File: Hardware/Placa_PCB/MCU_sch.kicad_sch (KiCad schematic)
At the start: 0 parts

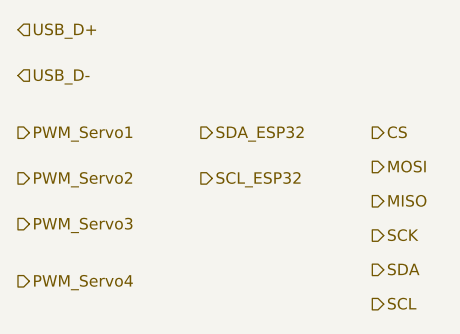
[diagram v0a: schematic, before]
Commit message: Agregando Level Shifter al PWM del Servo
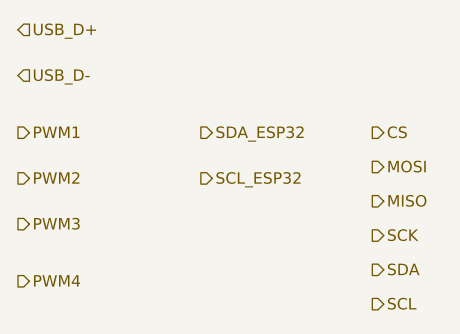
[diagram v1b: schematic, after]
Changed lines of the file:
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@@
 		)
 	)
-	(hierarchical_label "PWM_Servo4"
+	(hierarchical_label "PWM4"
 		(shape output)
 		(at 62.23 88.9 0)
@@
 		)
 	)
-	(hierarchical_label "PWM_Servo1"
+	(hierarchical_label "PWM1"
 		(shape output)
 		(at 62.23 72.39 0)
@@
 		)
 	)
-	(hierarchical_label "PWM_Servo3"
+	(hierarchical_label "PWM3"
 		(shape output)
 		(at 62.23 82.55 0)
@@
 		)
 	)
-	(hierarchical_label "PWM_Servo2"
+	(hierarchical_label "PWM2"
 		(shape output)
 		(at 62.23 77.47 0)

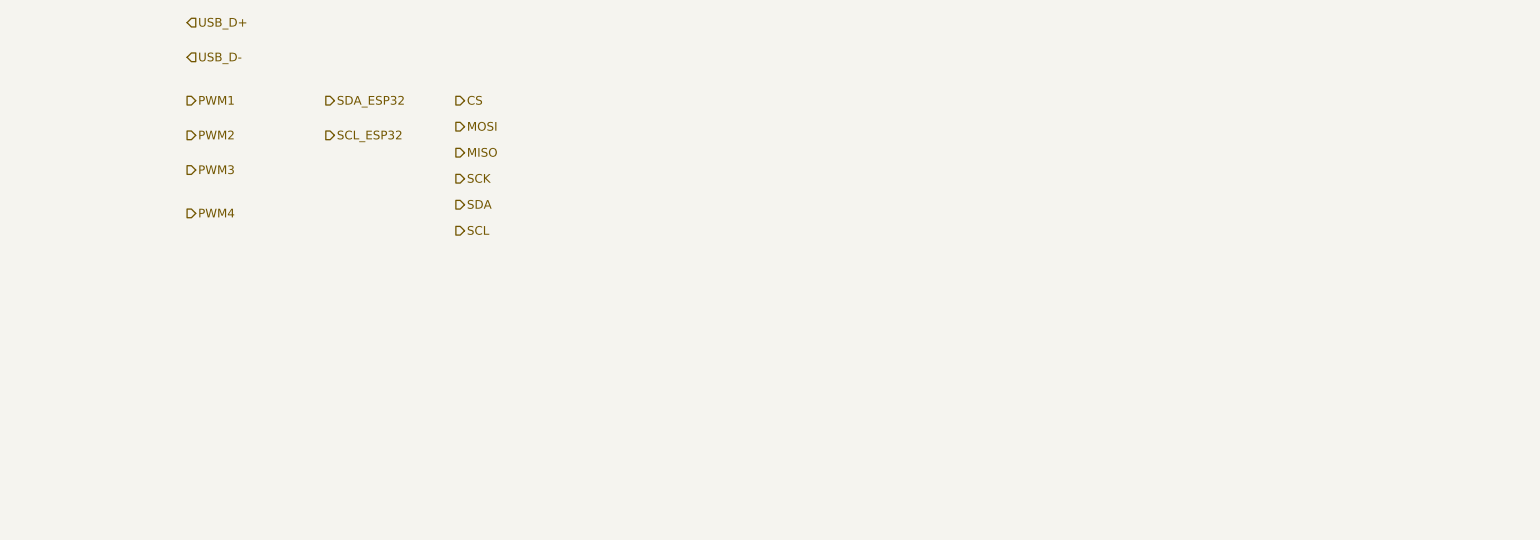
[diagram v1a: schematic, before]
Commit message: Agregando MCU al esquematico
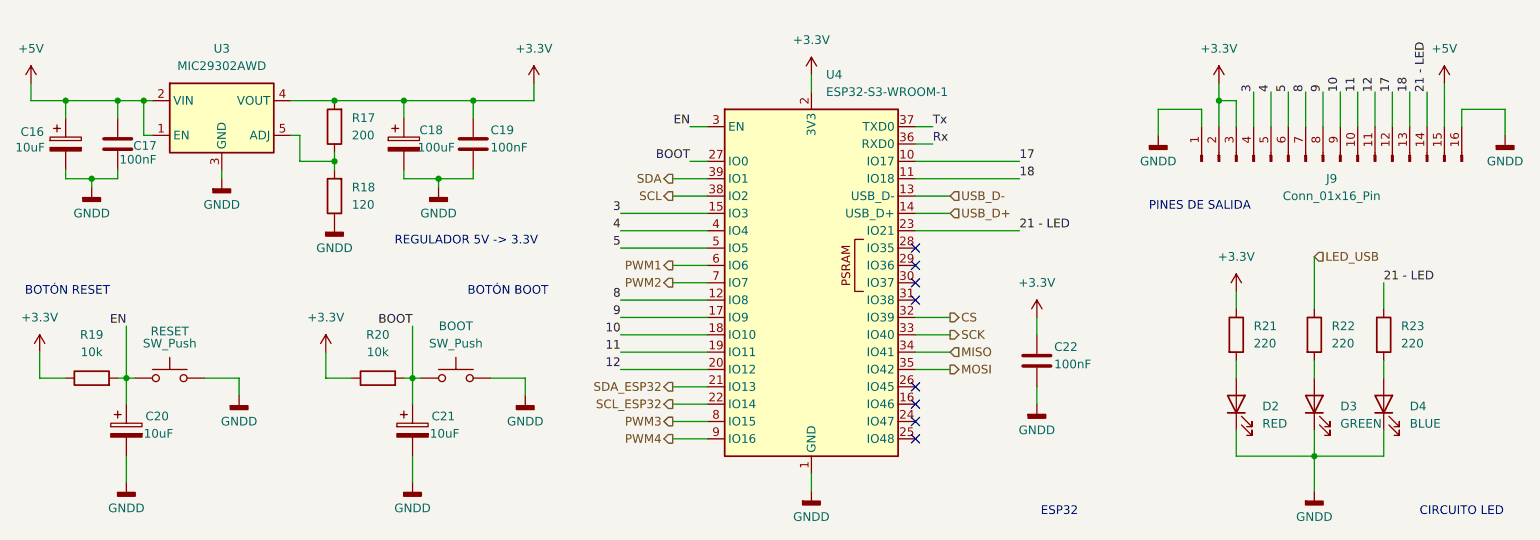
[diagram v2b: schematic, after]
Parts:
- added BOOT, RESET: SW_Push, Button_Switch_SMD:SW_SPST_TL3342, symbol Switch:SW_Push
- added C16, C20, C21: 10uF, symbol Device:C_Polarized
- added C17, C19, C22: 100nF, symbol Device:C
- added C18: 100uF, symbol Device:C_Polarized
- added D2: RED, symbol Device:LED
- added D3: GREEN, symbol Device:LED
- added D4: BLUE, symbol Device:LED
- added J9: Conn_01x16_Pin, symbol Connector:Conn_01x16_Pin
- added R17: 200, symbol Device:R
- added R18: 120, symbol Device:R
- added R19, R20: 10k, symbol Device:R
- added R21, R22, R23: 220, symbol Device:R
- added U3: MIC29302AWD, Package_TO_SOT_SMD:TO-252-5_TabPin3, symbol Regulator_Linear:MIC29302AWD
- added U4: ESP32-S3-WROOM-1, RF_Module:ESP32-S3-WROOM-1, symbol RF_Module:ESP32-S3-WROOM-1
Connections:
- net CS: now also U4.32 (IO39)
- net MISO: now also U4.34 (IO41)
- net MOSI: now also U4.35 (IO42)
- net PWM1: now also U4.6 (IO6)
- net PWM2: now also U4.7 (IO7)
- net PWM3: now also U4.8 (IO15)
- net PWM4: now also U4.9 (IO16)
- net SCK: now also U4.33 (IO40)
- net SCL: now also U4.38 (IO2)
- net SCL_ESP32: now also U4.22 (IO14)
- net SDA: now also U4.39 (IO1)
- net SDA_ESP32: now also U4.21 (IO13)
- net USB_D+: now also U4.14 (USB_D+)
- net USB_D-: now also U4.13 (USB_D-)
- new net: R17.1, R18.2, U3.5 (ADJ)
- new net: D2.2 (A), R21.2
- new net: D4.2 (A), R23.2
- new net: D3.2 (A), R22.2
- new net +3.3V: C18.1, C19.1, C22.1, J9.2 (Pin_2), J9.3 (Pin_3), R17.2, R19.1, R20.1, R21.1, U3.4 (VOUT), U4.2 (3V3)
- new net +5V: C16.1, C17.1, J9.15 (Pin_15), U3.1 (EN), U3.2 (VIN)
- new net 10: J9.9 (Pin_9), U4.18 (IO10)
- new net 11: J9.10 (Pin_10), U4.19 (IO11)
- new net 12: J9.11 (Pin_11), U4.20 (IO12)
- new net 17: J9.12 (Pin_12), U4.10 (IO17)
- new net 18: J9.13 (Pin_13), U4.11 (IO18)
- new net 21 - LED: J9.14 (Pin_14), R23.1, U4.23 (IO21)
- new net 3: J9.4 (Pin_4), U4.15 (IO3)
- new net 4: J9.5 (Pin_5), U4.4 (IO4)
- new net 5: J9.6 (Pin_6), U4.5 (IO5)
- new net 8: J9.7 (Pin_7), U4.12 (IO8)
- new net 9: J9.8 (Pin_8), U4.17 (IO9)
- new net BOOT: BOOT.1, C21.1, R20.2, U4.27 (IO0)
- new net EN: C20.1, R19.2, RESET.1, U4.3 (EN)
- new net GNDD: BOOT.2, C16.2, C17.2, C18.2, C19.2, C20.2, C21.2, C22.2, D2.1 (K), D3.1 (K), D4.1 (K), J9.1 (Pin_1), J9.16 (Pin_16), R18.1, RESET.2, U3.3 (GND), U4.1 (GND), U4.40 (GND), U4.41 (GND)
- new net LED_USB: R22.1
- new net Rx: U4.36 (RXD0)
- new net Tx: U4.37 (TXD0)
- no-connect marks 0 -> 8
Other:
- note added: "BOTÓN BOOT"
- note added: "BOTÓN RESET"
- note added: "CIRCUITO LED"
- note added: "ESP32"
- note added: "PINES DE SALIDA"
- note added: "REGULADOR 5V -> 3.3V"

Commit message: Esquematico Final
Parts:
- removed C18: 100uF, symbol Device:C_Polarized
- removed C20, C21: 10uF, symbol Device:C_Polarized
- removed J9: Conn_01x16_Pin, symbol Connector:Conn_01x16_Pin
- added C19, C20: 10uF, Capacitor_SMD:C_0805_2012Metric_Pad1.18x1.45mm_HandSolder, symbol Device:C
- added J9: Conn_01x18_Pin, Connector_PinSocket_2.54mm:PinSocket_1x18_P2.54mm_Vertical, symbol Connector:Conn_01x18_Pin
- 3V3_POW1: renamed from D2; value RED -> GREEN; footprint (none) -> LED_SMD:LED_0805_2012Metric_Pad1.15x1.40mm_HandSolder
- 5V_POW1: renamed from D3; value GREEN -> ORANGE; footprint (none) -> LED_SMD:LED_0805_2012Metric_Pad1.15x1.40mm_HandSolder
- BOOT1: renamed from BOOT; footprint Button_Switch_SMD:SW_SPST_TL3342 -> Button_Switch_SMD:SW_Push_1P1T_NO_E-Switch_TL3301NxxxxxG
- C16, C17: footprint (none) -> Capacitor_SMD:C_0805_2012Metric_Pad1.18x1.45mm_HandSolder
- C18: renamed from C19; footprint (none) -> Capacitor_SMD:CP_Elec_6.3x5.8
- C21: renamed from C22; footprint (none) -> Capacitor_SMD:C_0805_2012Metric_Pad1.18x1.45mm_HandSolder
- PIN21: renamed from D4; value BLUE -> YELLOW; footprint (none) -> LED_SMD:LED_0805_2012Metric_Pad1.15x1.40mm_HandSolder
- R17, R18, R19, R20: footprint (none) -> Resistor_SMD:R_0805_2012Metric_Pad1.20x1.40mm_HandSolder
- R21: value 220 -> 100; footprint (none) -> Resistor_SMD:R_0805_2012Metric_Pad1.20x1.40mm_HandSolder
- R22: value 220 -> 330; footprint (none) -> Resistor_SMD:R_0805_2012Metric_Pad1.20x1.40mm_HandSolder
- R23: value 220 -> 120; footprint (none) -> Resistor_SMD:R_0805_2012Metric_Pad1.20x1.40mm_HandSolder
- RESET1: renamed from RESET; footprint Button_Switch_SMD:SW_SPST_TL3342 -> Button_Switch_SMD:SW_Push_1P1T_NO_E-Switch_TL3301NxxxxxG
- renumbered U3 to U4, U4 to U5
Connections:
- net 12 is gone; now on net SDA: U5.20 (IO12)
- net 4 is gone; now on net PWM1: U5.4 (IO4)
- net 5 is gone; now on net PWM2: U5.5 (IO5)
- net +3.3V: now also J9.2 (Pin_2), J9.3 (Pin_3)
- net +5V: now also J9.16 (Pin_16), J9.17 (Pin_17)
- net 10: now also J9.7 (Pin_7)
- net 11: now also J9.8 (Pin_8)
- net 17: now also J9.11 (Pin_11)
- net 18: now also J9.12 (Pin_12)
- net 3: now also J9.4 (Pin_4)
- net 8: now also J9.5 (Pin_5)
- net 9: now also J9.6 (Pin_6)
- net BOOT: now also C20.1
- net CS: now also U5.24 (IO47); no longer U5.32 (IO39)
- net EN: now also C19.1
- net GNDD: now also C19.2, C20.2, J9.1 (Pin_1), J9.18 (Pin_18)
- net MISO: now also U5.23 (IO21); no longer U5.34 (IO41)
- net MOSI: now also U5.22 (IO14); no longer U5.35 (IO42)
- net PWM1: no longer U5.6 (IO6)
- net PWM2: no longer U5.7 (IO7)
- net PWM3: now also U5.6 (IO6); no longer U5.8 (IO15)
- net PWM4: now also U5.7 (IO7); no longer U5.9 (IO16)
- net SCK: now also U5.25 (IO48); no longer U5.33 (IO40)
- net SCL: now also U5.21 (IO13); no longer U5.38 (IO2)
- net SCL_ESP32: now also U5.38 (IO2); no longer U5.22 (IO14)
- net SDA: no longer U5.39 (IO1)
- net SDA_ESP32: now also U5.39 (IO1); no longer U5.21 (IO13)
- net 38 - LED: now reaches U5.31 (IO38)
- net 38 - LED: now also R23.1, J9.13 (Pin_13)
- removed net 21 - LED: R23.1, U5.23 (IO21)
- net Rx renamed RX
- net RX: now also J9.15 (Pin_15)
- net Tx renamed TX
- net TX: now also J9.14 (Pin_14)
- new net 15: J9.9 (Pin_9), U5.8 (IO15)
- new net 16: J9.10 (Pin_10), U5.9 (IO16)
- no-connect marks 8 -> 9
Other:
- moved on the sheet: C18

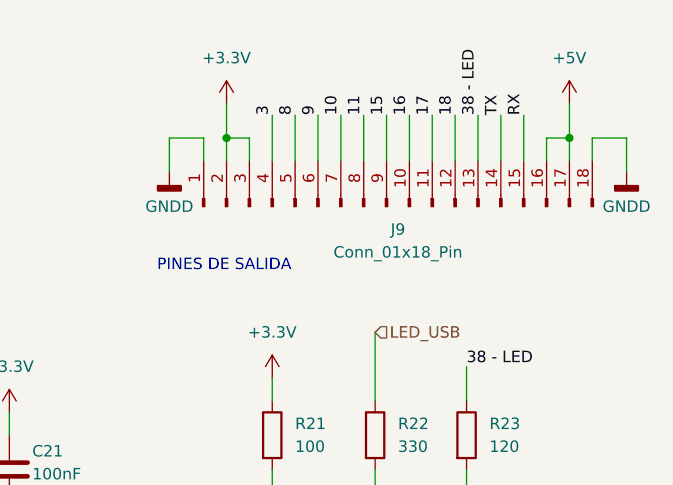
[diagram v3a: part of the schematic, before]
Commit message: Agregando huella del capacitor de 10uF y comenzando con el PCB (USB + Alimentacion)
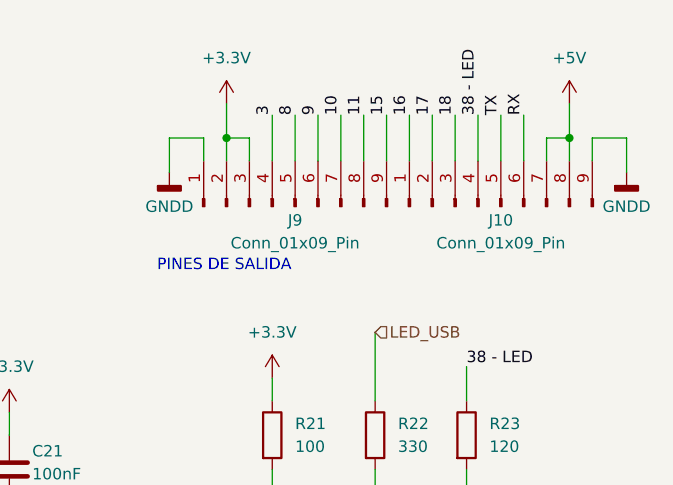
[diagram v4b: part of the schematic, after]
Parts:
- removed J9: Conn_01x18_Pin, Connector_PinSocket_2.54mm:PinSocket_1x18_P2.54mm_Vertical, symbol Connector:Conn_01x18_Pin
- added J10, J9: Conn_01x09_Pin, Connector_PinSocket_2.54mm:PinSocket_1x09_P2.54mm_Vertical, symbol Connector:Conn_01x09_Pin
- C16: footprint Capacitor_SMD:C_0805_2012Metric_Pad1.18x1.45mm_HandSolder -> Capacitor_SMD:CP_Elec_4x5.4
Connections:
- net +3.3V: now also J9.2 (Pin_2), J9.3 (Pin_3)
- net +5V: now also J10.7 (Pin_7), J10.8 (Pin_8)
- net 10: now also J9.7 (Pin_7)
- net 11: now also J9.8 (Pin_8)
- net 15: now also J9.9 (Pin_9)
- net 16: now also J10.1 (Pin_1)
- net 17: now also J10.2 (Pin_2)
- net 18: now also J10.3 (Pin_3)
- net 3: now also J9.4 (Pin_4)
- net 38 - LED: now also J10.4 (Pin_4)
- net 8: now also J9.5 (Pin_5)
- net 9: now also J9.6 (Pin_6)
- net GNDD: now also J10.9 (Pin_9), J9.1 (Pin_1)
- net RX: now also J10.6 (Pin_6)
- net TX: now also J10.5 (Pin_5)

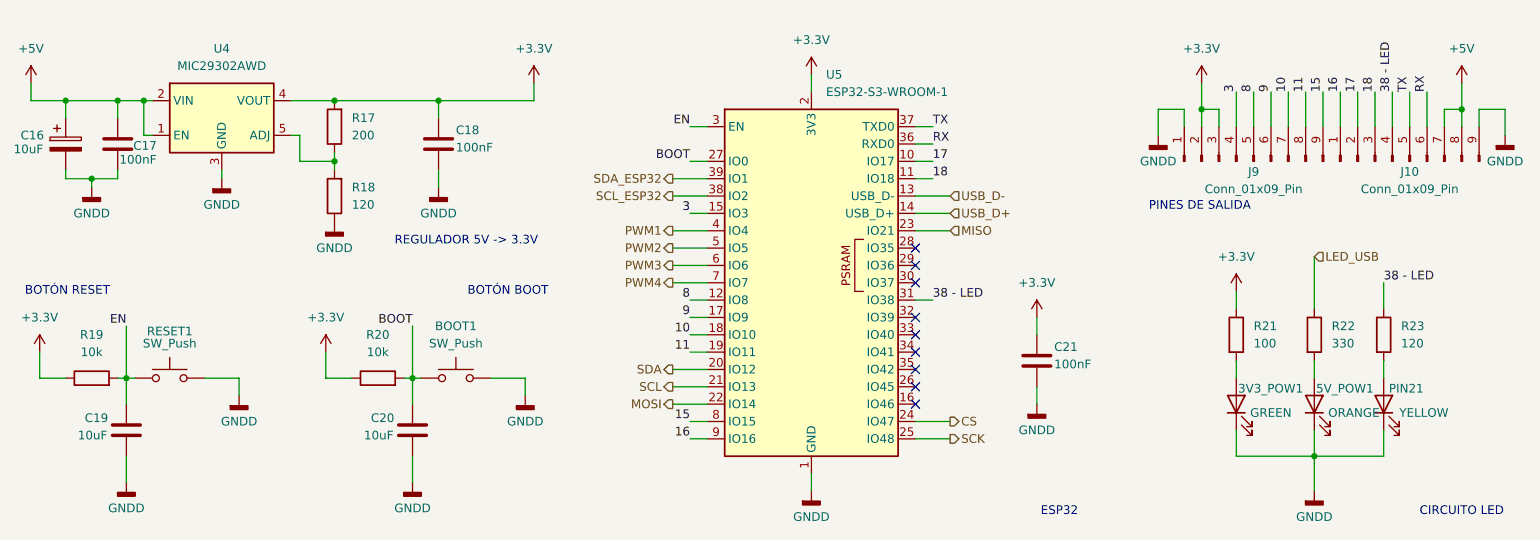
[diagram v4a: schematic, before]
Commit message: Acomodando los componentes en el PCB y cambiendo las conexiones con el ESP32
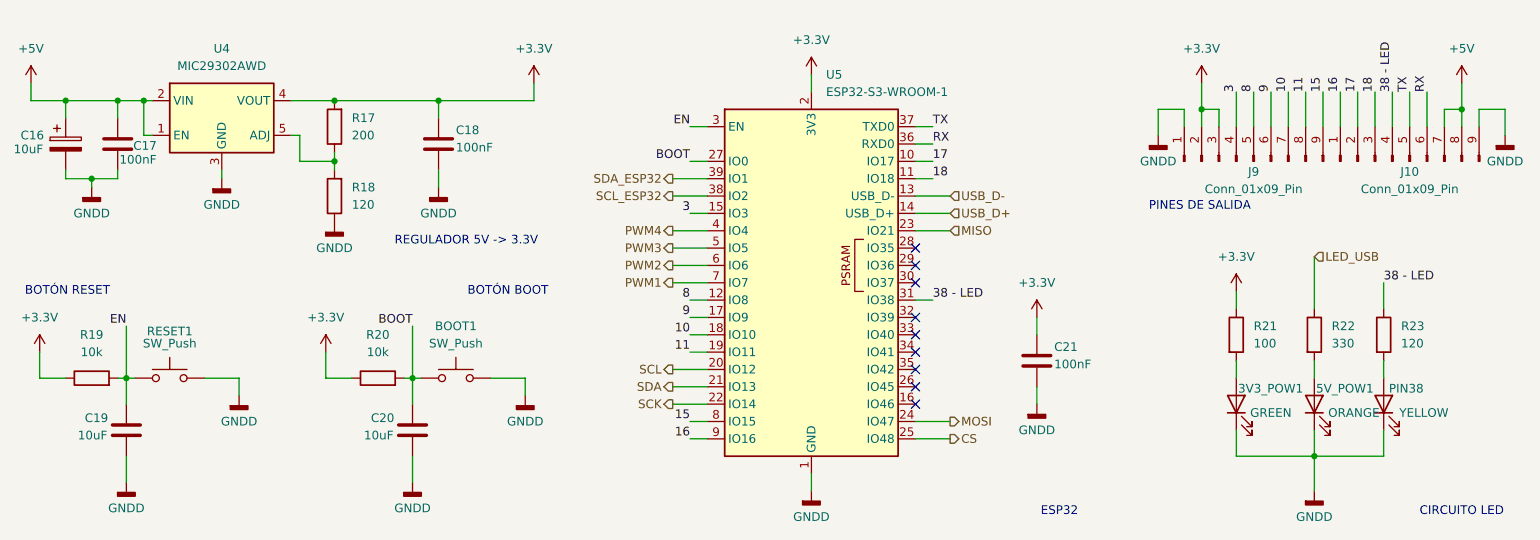
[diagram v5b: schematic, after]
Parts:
- C18: footprint Capacitor_SMD:CP_Elec_6.3x5.8 -> Capacitor_SMD:C_0805_2012Metric_Pad1.18x1.45mm_HandSolder
- renumbered PIN21 to PIN38
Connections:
- net CS: now also U5.25 (IO48); no longer U5.24 (IO47)
- net MOSI: now also U5.24 (IO47); no longer U5.22 (IO14)
- net PWM1: now also U5.7 (IO7); no longer U5.4 (IO4)
- net PWM2: now also U5.6 (IO6); no longer U5.5 (IO5)
- net PWM3: now also U5.5 (IO5); no longer U5.6 (IO6)
- net PWM4: now also U5.4 (IO4); no longer U5.7 (IO7)
- net SCK: now also U5.22 (IO14); no longer U5.25 (IO48)
- net SCL: now also U5.20 (IO12); no longer U5.21 (IO13)
- net SDA: now also U5.21 (IO13); no longer U5.20 (IO12)
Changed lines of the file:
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@@
 	(wire
 		(pts
-			(xy 255.27 73.66) (xy 251.46 73.66)
+			(xy 133.35 99.06) (xy 138.43 99.06)
 		)
 		(stroke
@@
 	(wire
 		(pts
-			(xy 135.89 106.68) (xy 138.43 106.68)
+			(xy 255.27 73.66) (xy 251.46 73.66)
 		)
 		(stroke
@@
 	(wire
 		(pts
-			(xy 248.92 69.85) (xy 248.92 73.66)
+			(xy 135.89 106.68) (xy 138.43 106.68)
 		)
 		(stroke
@@
 	(wire
 		(pts
-			(xy 227.33 124.46) (xy 227.33 129.54)
+			(xy 248.92 69.85) (xy 248.92 73.66)
 		)
 		(stroke
@@
 	(wire
 		(pts
-			(xy 135.89 81.28) (xy 138.43 81.28)
+			(xy 227.33 124.46) (xy 227.33 129.54)
 		)
 		(stroke
@@
 	(wire
 		(pts
-			(xy 133.35 116.84) (xy 138.43 116.84)
+			(xy 135.89 81.28) (xy 138.43 81.28)
 		)
 		(stroke
@@
 	(wire
 		(pts
-			(xy 237.49 110.49) (xy 237.49 113.03)
+			(xy 133.35 116.84) (xy 138.43 116.84)
 		)
 		(stroke
@@
 	(wire
 		(pts
-			(xy 133.35 93.98) (xy 138.43 93.98)
+			(xy 237.49 110.49) (xy 237.49 113.03)
 		)
 		(stroke
@@
 	(wire
 		(pts
-			(xy 133.35 91.44) (xy 138.43 91.44)
-		)
-		(stroke
-			(width 0)
-			(type default)
-		)
-	)
-	(wire
-		(pts
 			(xy 83.82 72.39) (xy 99.06 72.39)
 		)
@@
 	(wire
 		(pts
+			(xy 133.35 93.98) (xy 138.43 93.98)
+		)
+		(stroke
+			(width 0)
+			(type default)
+		)
+	)
+	(wire
+		(pts
 			(xy 106.68 113.03) (xy 111.76 113.03)
 		)
@@
 	(wire
 		(pts
-			(xy 133.35 99.06) (xy 138.43 99.06)
-		)
-		(stroke
-			(width 0)
-			(type default)
-		)
-	)
-	(wire
-		(pts
 			(xy 78.74 77.47) (xy 78.74 81.28)
 		)
@@
 	(wire
 		(pts
-			(xy 133.35 96.52) (xy 138.43 96.52)
-		)
-		(stroke
-			(width 0)
-			(type default)
-		)
-	)
-	(wire
-		(pts
 			(xy 44.45 83.82) (xy 48.26 83.82)
 		)
@@
 	(wire
 		(pts
+			(xy 133.35 96.52) (xy 138.43 96.52)
+		)
+		(stroke
+			(width 0)
+			(type default)
+		)
+	)
+	(wire
+		(pts
 			(xy 231.14 71.12) (xy 231.14 76.2)
 		)
@@
 	(wire
 		(pts
+			(xy 133.35 91.44) (xy 138.43 91.44)
+		)
+		(stroke
+			(width 0)
+			(type default)
+		)
+	)
+	(wire
+		(pts
 			(xy 48.26 83.82) (xy 48.26 85.09)
 		)
@@
 	(hierarchical_label "PWM4"
 		(shape output)
-		(at 133.35 99.06 180)
+		(at 133.35 91.44 180)
 		(effects
 			(font
@@
 	(hierarchical_label "SDA"
 		(shape output)
-		(at 133.35 111.76 180)
+		(at 133.35 114.3 180)
 		(effects
 			(font
@@
 	(hierarchical_label "CS"
 		(shape output)
-		(at 173.99 119.38 0)
+		(at 173.99 121.92 0)
 		(effects
 			(font
@@
 	(hierarchical_label "MOSI"
 		(shape output)
-		(at 133.35 116.84 180)
+		(at 173.99 119.38 0)
 		(effects
 			(font
 				(size 1.27 1.27)
 			)
-			(justify right)
+			(justify left)
 		)
 	)
@@
 	(hierarchical_label "PWM1"
 		(shape output)
-		(at 133.35 91.44 180)
+		(at 133.35 99.06 180)
 		(effects
 			(font
@@
 	(hierarchical_label "SCL"
 		(shape output)
-		(at 133.35 114.3 180)
+		(at 133.35 111.76 180)
 		(effects
 			(font
@@
 	(hierarchical_label "PWM2"
 		(shape output)
-		(at 133.35 93.98 180)
+		(at 133.35 96.52 180)
 		(effects
 			(font
@@
 	(hierarchical_label "SCK"
 		(shape output)
-		(at 173.99 121.92 0)
+		(at 133.35 116.84 180)
 		(effects
 			(font
 				(size 1.27 1.27)
 			)
-			(justify left)
+			(justify right)
 		)
 	)
 	(hierarchical_label "PWM3"
 		(shape output)
-		(at 133.35 96.52 180)
+		(at 133.35 93.98 180)
 		(effects
 			(font
@@
 		(on_board yes)
 		(dnp no)
-		(property "Reference" "PIN21"
+		(property "Reference" "PIN38"
 			(at 238.252 114.554 90)
 			(effects
@@
 			(project "ScramblerBot"
 				(path "/ca162c4b-e7f6-494c-9ea1-0d86ef4a8e44/adcfffa9-f2fe-4426-b325-243cee8602ce"
-					(reference "PIN21")
+					(reference "PIN38")
 					(unit 1)
 				)
@@
 			)
 		)
-		(property "Footprint" "Capacitor_SMD:CP_Elec_6.3x5.8"
+		(property "Footprint" "Capacitor_SMD:C_0805_2012Metric_Pad1.18x1.45mm_HandSolder"
 			(at 100.0252 82.55 0)
 			(effects

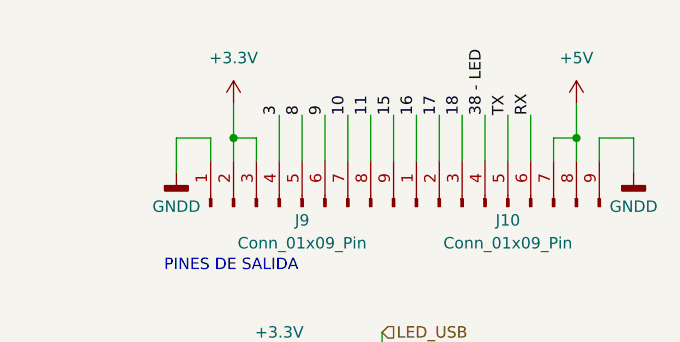
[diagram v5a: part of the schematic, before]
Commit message: Terminando el enrutado de los +5V y comenzando las pistas de 3.3V
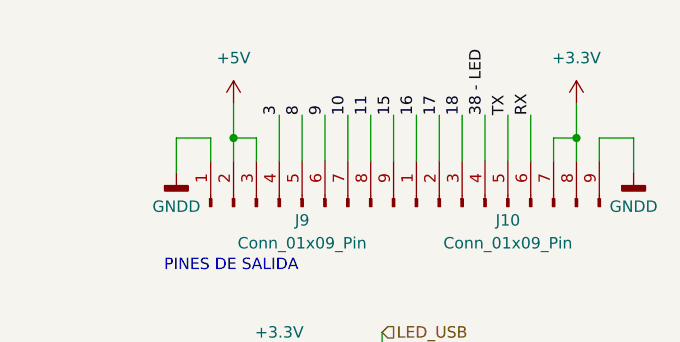
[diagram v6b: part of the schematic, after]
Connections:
- net +3.3V: now also J10.7 (Pin_7), J10.8 (Pin_8); no longer J9.2 (Pin_2), J9.3 (Pin_3)
- net +5V: now also J9.2 (Pin_2), J9.3 (Pin_3); no longer J10.7 (Pin_7), J10.8 (Pin_8)
